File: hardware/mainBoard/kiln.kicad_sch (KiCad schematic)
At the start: 0 parts

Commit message: Safety link: the isolated UART pin map, measured instead of traced
The ESP's safety-link TX/RX were swapped relative to the board, and had
been since the pin defaults were set. The link could not work in either
direction: the ESP transmitted into U3's collector and listened on U2's
LED drive. Correct map, now measured on the bench rather than derived
from the schematic:

  ESP GPIO5 = TX (DataToSafty, drives U2's LED through R12)
  ESP GPIO4 = RX (DataFromSafty, U3's collector, R15 pull-up)

Schematic and board
-------------------
Three faults, all fixed here and reworked on the physical board:

  - The top-level sheet crossed the two hierarchical pins: MainControler's
    DataToSafty (an output) was wired to SaftyProcessor's DataFromSafty
    (also an output), and the two inputs were wired to each other. That
    collapsed the two names into one net, which KiCad named after the
    main sheet, so the same wire appeared under both names depending on
    which sheet you read.
  - The MainControler sheet's labels were swapped relative to the safety
    sheet's. They now agree: U3's collector is DataFromSafty everywhere,
    R12's net is DataToSafty everywhere.
  - R15 (1k to 3.3V_Main) sat on the TX net, where a pull-up does nothing,
    while the RX collector had none. Moved onto GPIO4, mirroring R9's role
    on the safety side.

The measurement
---------------
Coordinated two-board GPIO test, each processor reached by a path that is
not the link under test (ESP over its USB-serial bridge and JTAG, Pico
over SWD). Every crossing inverts, as predicted:

  ESP GPIO5 high  -> Pico GP5 low    (U2's LED lit)
  ESP GPIO5 low   -> Pico GP5 high   (R9 pulls up)
  Pico GP4 high   -> ESP GPIO4 low   (U3's LED lit)
  Pico GP4 low    -> ESP GPIO4 high  (R15 pulls up)
  Pico GP5 driven -> no change at the ESP (its own receiver)
  ESP GPIO6 high  -> Pico GP10 low   (U1's LED lit)
  ESP in reset    -> Pico GP10 high  (R8 pulls up)

Corroborated at register level: ESP GPIO_IN_REG 0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
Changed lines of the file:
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@@
 			)
 		)
-		(pin "DataFromSafty" input
+		(pin "DataToSafty" output
 			(at 101.6 105.41 0)
 			(effects
@@
 			)
 		)
-		(pin "DataToSafty" output
+		(pin "DataFromSafty" input
 			(at 101.6 107.95 0)
 			(effects

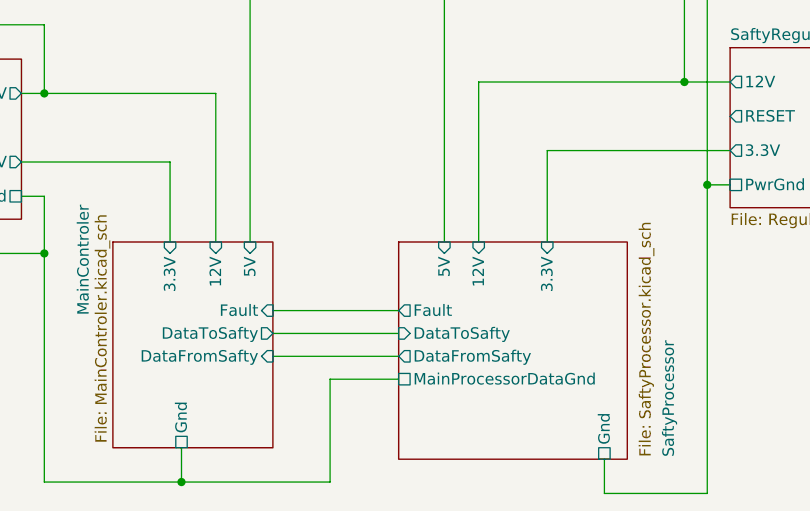
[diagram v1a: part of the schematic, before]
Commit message: Safety link: ADuM1201 replaces the optocouplers, and 9600 was never our limit
The TCMT1109 pair (U2/U3 with R7/R12/R15) that carried the ESP<->RP2040
UART is gone, replaced by one ADuM1201WT digital isolator, U6. Two
properties of that part drove every firmware change here:

  - It does not invert. Each optocoupler did, which is why both ends
    inverted their own TX to cancel it. With a non-inverting barrier
    those cancellations have nothing to cancel, so keeping either one
    parks the far end's RX in a permanent break. Measured with the
    isolator fitted and the old inversions still in place: sent 18,
    received 0, crc/framing errors 33 and climbing, Pico RX pad low on
    2954 of 3000 samples. Both inversions removed:
    uart_set_line_inverse(TXD_INV) from safety_link.c and
    gpio_set_outover(GPIO_OVERRIDE_INVERT) from uart_owner.c.

  - It is fast. The 9600 ceiling was a property of the optocouplers, not
    of either firmware, and every doc that said otherwise was wrong.
    A descending sweep of the standard rates, 60s continuous per rate,
    judged on crc/framing + length-mismatch + crc-mismatch + resync
    deltas: 921600, 460800 and 230400 all clean, zero new errors, status
    replies answering every 500ms poll. Committed value is 230400 -- one
    standard step below the fastest pass is 460800, and 230400 is the
    slower of that and the requested 230400. Two full standard steps of
    margin below a rate that soaks clean.

Also found, while reading the code this change touches: the bootloader's
recovery mode never applied the TX inversion the application did, and its
comment claimed the two matched. Under the optocouplers recovery mode's
Pico->ESP polarity was therefore inverted relative to the application.
Both are non-inverting now, so recovery mode is correct for the first
time -- documented in bootloader/main.c rather than silently fixed.

Baud is hardcoded in three places that must agree, now called out in each:
KilnFW's KILNCTL_SAFET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
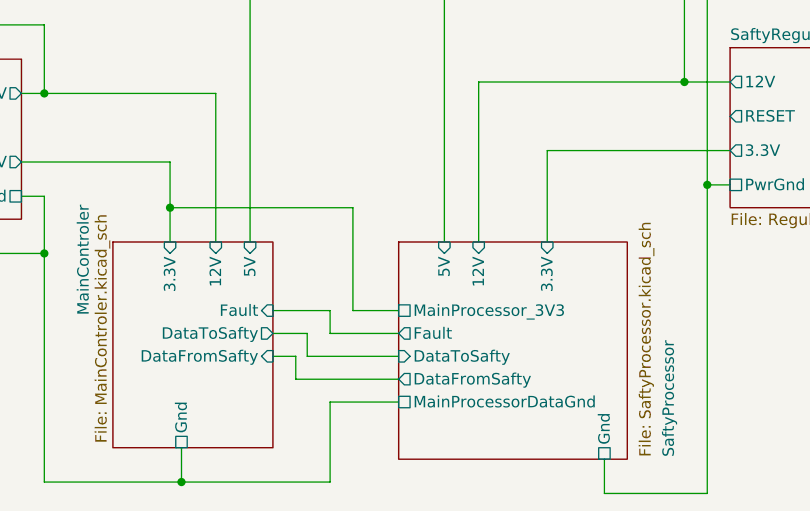
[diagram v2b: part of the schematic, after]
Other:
- sheet SaftyProcessor ports: added MainProcessor_3V3; removed none
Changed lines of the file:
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@@
+	)
+	(junction
+		(at 90.17 91.44)
+		(diameter 0)
+		(color 0 0 0 0)
 	)
 	(junction
@@
 	(wire
 		(pts
-			(xy 115.57 107.95) (xy 101.6 107.95)
+			(xy 110.49 91.44) (xy 90.17 91.44)
+		)
+		(stroke
+			(width 0)
+			(type default)
+		)
+	)
+	(wire
+		(pts
+			(xy 115.57 110.49) (xy 104.14 110.49)
 		)
 		(stroke
@@
 	(wire
 		(pts
-			(xy 115.57 110.49) (xy 107.95 110.49)
+			(xy 115.57 113.03) (xy 107.95 113.03)
+		)
+		(stroke
+			(width 0)
+			(type default)
+		)
+	)
+	(wire
+		(pts
+			(xy 107.95 102.87) (xy 101.6 102.87)
 		)
 		(stroke
@@
 	(wire
 		(pts
-			(xy 115.57 102.87) (xy 101.6 102.87)
+			(xy 115.57 105.41) (xy 107.95 105.41)
 		)
 		(stroke
@@
 	(wire
 		(pts
+			(xy 105.41 107.95) (xy 105.41 105.41)
+		)
+		(stroke
+			(width 0)
+			(type default)
+		)
+	)
+	(wire
+		(pts
 			(xy 48.26 58.42) (xy 38.1 58.42)
 		)
@@
 	(wire
 		(pts
+			(xy 104.14 107.95) (xy 101.6 107.95)
+		)
+		(stroke
+			(width 0)
+			(type default)
+		)
+	)
+	(wire
+		(pts
 			(xy 149.86 62.23) (xy 153.67 62.23)
 		)
@@
 	(wire
 		(pts
-			(xy 107.95 110.49) (xy 107.95 121.92)
+			(xy 110.49 102.87) (xy 110.49 91.44)
+		)
+		(stroke
+			(width 0)
+			(type default)
+		)
+	)
+	(wire
+		(pts
+			(xy 107.95 113.03) (xy 107.95 121.92)
+		)
+		(stroke
+			(width 0)
+			(type default)
+		)
+	)
+	(wire
+		(pts
+			(xy 104.14 110.49) (xy 104.14 107.95)
 		)
 		(stroke
@@
 	(wire
 		(pts
+			(xy 90.17 91.44) (xy 90.17 95.25)
+		)
+		(stroke
+			(width 0)
+			(type default)
+		)
+	)
+	(wire
+		(pts
 			(xy 76.2 71.12) (xy 76.2 78.74)
 		)
@@
 	(wire
 		(pts
-			(xy 115.57 105.41) (xy 101.6 105.41)
+			(xy 115.57 107.95) (xy 105.41 107.95)
 		)
 		(stroke
@@
 	(wire
 		(pts
-			(xy 90.17 86.36) (xy 90.17 95.25)
+			(xy 90.17 86.36) (xy 90.17 91.44)
 		)
 		(stroke
@@
 	(wire
 		(pts
+			(xy 105.41 105.41) (xy 101.6 105.41)
+		)
+		(stroke
+			(width 0)
+			(type default)
+		)
+	)
+	(wire
+		(pts
 			(xy 138.43 123.19) (xy 149.86 123.19)
 		)
@@
 	(wire
 		(pts
+			(xy 115.57 102.87) (xy 110.49 102.87)
+		)
+		(stroke
+			(width 0)
+			(type default)
+		)
+	)
+	(wire
+		(pts
 			(xy 76.2 90.17) (xy 73.66 90.17)
 		)
@@
 		(pts
 			(xy 149.86 123.19) (xy 149.86 88.9)
+		)
+		(stroke
+			(width 0)
+			(type default)
+		)
+	)
+	(wire
+		(pts
+			(xy 107.95 105.41) (xy 107.95 102.87)
 		)
 		(stroke
@@
 		)
 		(pin "DataFromSafty" output
+			(at 115.57 110.49 180)
+			(effects
+				(font
+					(size 1.27 1.27)
+				)
+				(justify left)
+			)
+		)
+		(pin "DataToSafty" input
 			(at 115.57 107.95 180)
 			(effects
@@
 			)
 		)
-		(pin "DataToSafty" input
+		(pin "Fault" output
 			(at 115.57 105.41 180)
-			(effects
-				(font
-					(size 1.27 1.27)
-				)
-				(justify left)
-			)
-		)
-		(pin "Fault" output
-			(at 115.57 102.87 180)
 			(effects
 				(font
@@
 		)
 		(pin "MainProcessorDataGnd" passive
-			(at 115.57 110.49 180)
+			(at 115.57 113.03 180)
 			(effects
 				(font
@@
 			)
 		)
+		(pin "MainProcessor_3V3" passive
+			(at 115.57 102.87 180)
+			(effects
+				(font
+					(size 1.27 1.27)
+				)
+				(justify left)
+			)
+		)
